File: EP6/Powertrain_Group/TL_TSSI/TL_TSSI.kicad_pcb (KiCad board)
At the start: 2 copper layers, 80 x 18 mm, 15 parts

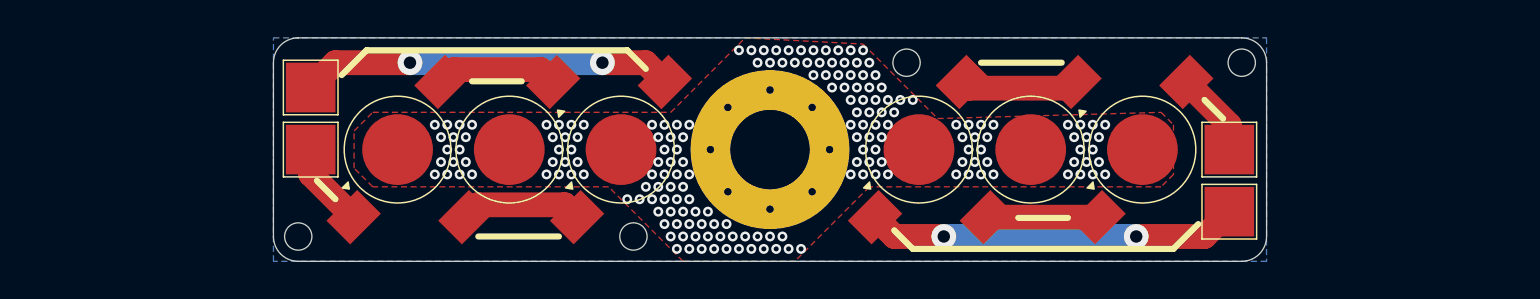
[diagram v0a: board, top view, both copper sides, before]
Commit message: update TL_TSSI to V1.2
V1.2 change mounting hole configureation
     (including removing middle hole and use M2 on 4 corner)
     increase LED count fron 3*2 to 6*2
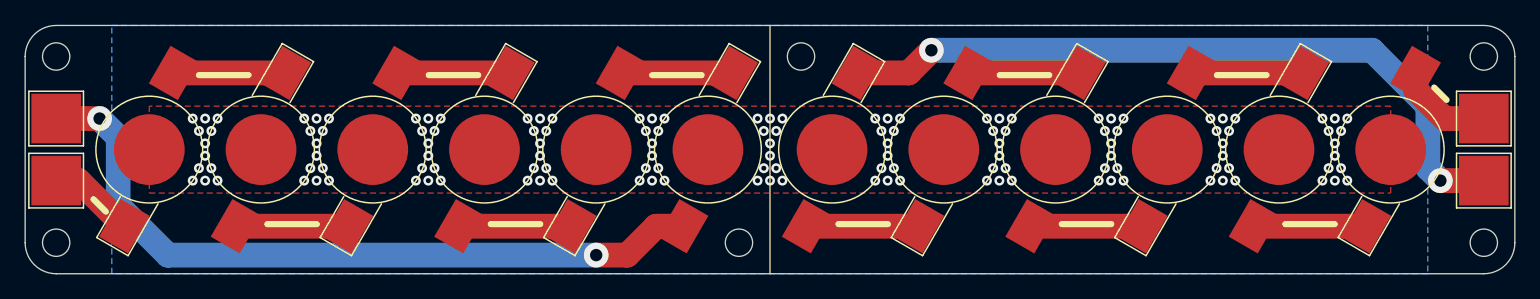
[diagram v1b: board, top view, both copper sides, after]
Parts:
- removed the H1 at (124.0, 60.0)
- added D10: GREEN, LED_SMD:LED_1W_3W_R8, F.Cu at (156.0, 60.0)
- added D11: GREEN, LED_SMD:LED_1W_3W_R8, F.Cu at (165.0, 60.0)
- added D12: GREEN, LED_SMD:LED_1W_3W_R8, F.Cu at (174.0, 60.0)
- added D4: RED, LED_SMD:LED_1W_3W_R8, F.Cu at (101.0, 60.0)
- added D5: RED, LED_SMD:LED_1W_3W_R8, F.Cu at (110.0, 60.0)
- added D6: RED, LED_SMD:LED_1W_3W_R8, F.Cu at (119.0, 60.0)
- added H5: MountingHole, MountingHole:MountingHole_2.2mm_M2, F.Cu at (126.5, 52.5)
- added H6: MountingHole, MountingHole:MountingHole_2.2mm_M2, F.Cu at (121.5, 67.5)
- H1: renamed from H2; value MountingHole_2.2mm_M2 -> MountingHole
- H2, H3: value MountingHole_2.2mm_M2 -> MountingHole
- H4: renamed from H3; value MountingHole_2.2mm_M2 -> MountingHole
- moved H1 70.0 mm to (181.5, 52.5)
- moved H3 68.5 mm to (66.5, 52.5)
- moved H4 24.3 mm to (181.5, 67.5)
- moved TP1 20.7 mm to (66.5, 62.5)
- moved TP2 20.7 mm to (66.5, 57.5)
- moved TP3 20.7 mm to (181.5, 62.5)
- moved TP4 20.7 mm to (181.5, 57.5)
- moved D1 20.0 mm to (74.0, 60.0), turned to 60 degrees
- moved D2 20.0 mm to (83.0, 60.0), turned to -120 degrees
- moved D3 20.0 mm to (92.0, 60.0), turned to 60 degrees
- moved H2 19.5 mm to (66.5, 67.5)
- moved D7 7.00 mm to (129.0, 60.0), turned to -120 degrees
- moved D8 7.00 mm to (138.0, 60.0), turned to 60 degrees
- moved D9 7.00 mm to (147.0, 60.0), turned to -120 degrees
- renumbered D4 to D7, D5 to D8, D6 to D9
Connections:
- D9 pad 2: Net-(D6-A) -> Net-(D10-K)
- TP2 pad 1: Net-(D3-A) -> Net-(D6-A)
- TP4 pad 1: Net-(D6-A) -> Net-(D12-A)
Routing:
- net Net-(D6-A): track 6.88 -> 59.2 mm, vias 0 -> 2
- net Net-(D7-K): track 30.0 -> 58.5 mm
- net Net-(D3-A): track 30.0 -> 9.00 mm, vias 2 -> 0
- net Net-(D5-A): track 0.00 -> 9.00 mm
- net Net-(D4-A): track 0.00 -> 9.00 mm
- net Net-(D11-A): track 0.00 -> 9.00 mm
- net Net-(D10-K): track 0.00 -> 9.00 mm
- net Net-(D10-A): track 0.00 -> 9.00 mm
- net Net-(D12-A): track 0.00 -> 7.81 mm
- net Net-(D1-A): track 9.83 -> 9.00 mm
- net Net-(D2-A): track 9.83 -> 9.00 mm
- net Earth: vias 180 -> 132
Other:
- board size 80 x 18 mm -> 120 x 20 mm
- board text added: "EP6 TL_TSSI"
- board text added: "Jack Kuo V1.2 25/06/15"
